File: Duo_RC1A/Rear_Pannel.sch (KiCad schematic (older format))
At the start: 61 parts, among them CN1 CONN_PANNEL, CN2 CONN_PANNEL, CN3 CONN_PANNEL, J10 MIDI_CONN, J11 JACK_3P_2.5MM, J6 USB_A, J7 MINI_USB_OTG, J8 RJ45_CHAIN, J9 MIDI_CONN, Q4 BS870, Q5 BS870, U5 RT9728BH, U6 RT9728BH, U7 6N137

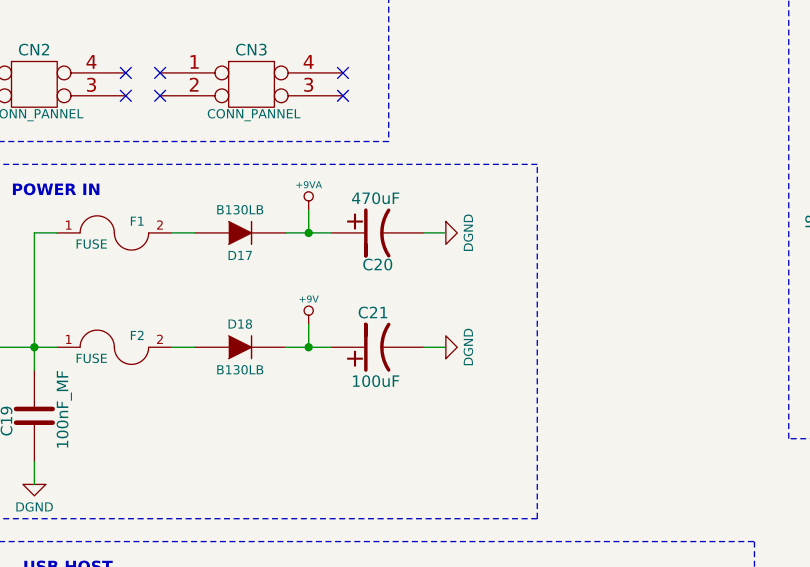
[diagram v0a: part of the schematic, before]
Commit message: PCB dimensions and group placement of all footprints on both BottomBoard and TopBoard layouts.
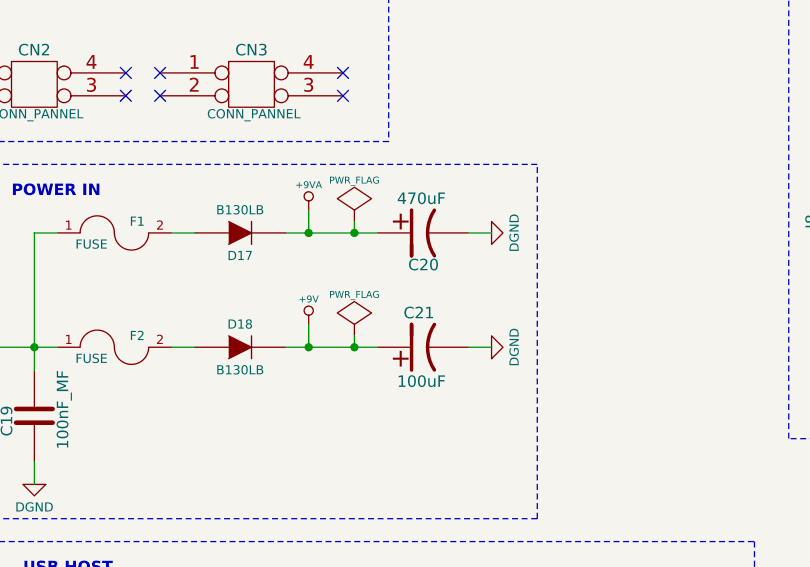
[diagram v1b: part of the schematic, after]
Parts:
- F1, F2: footprint Duo_Audio_HMI_RC1A:SM0603 -> Duo_Audio_HMI_RC1A:SM2920
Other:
- moved on the sheet: C20, C21

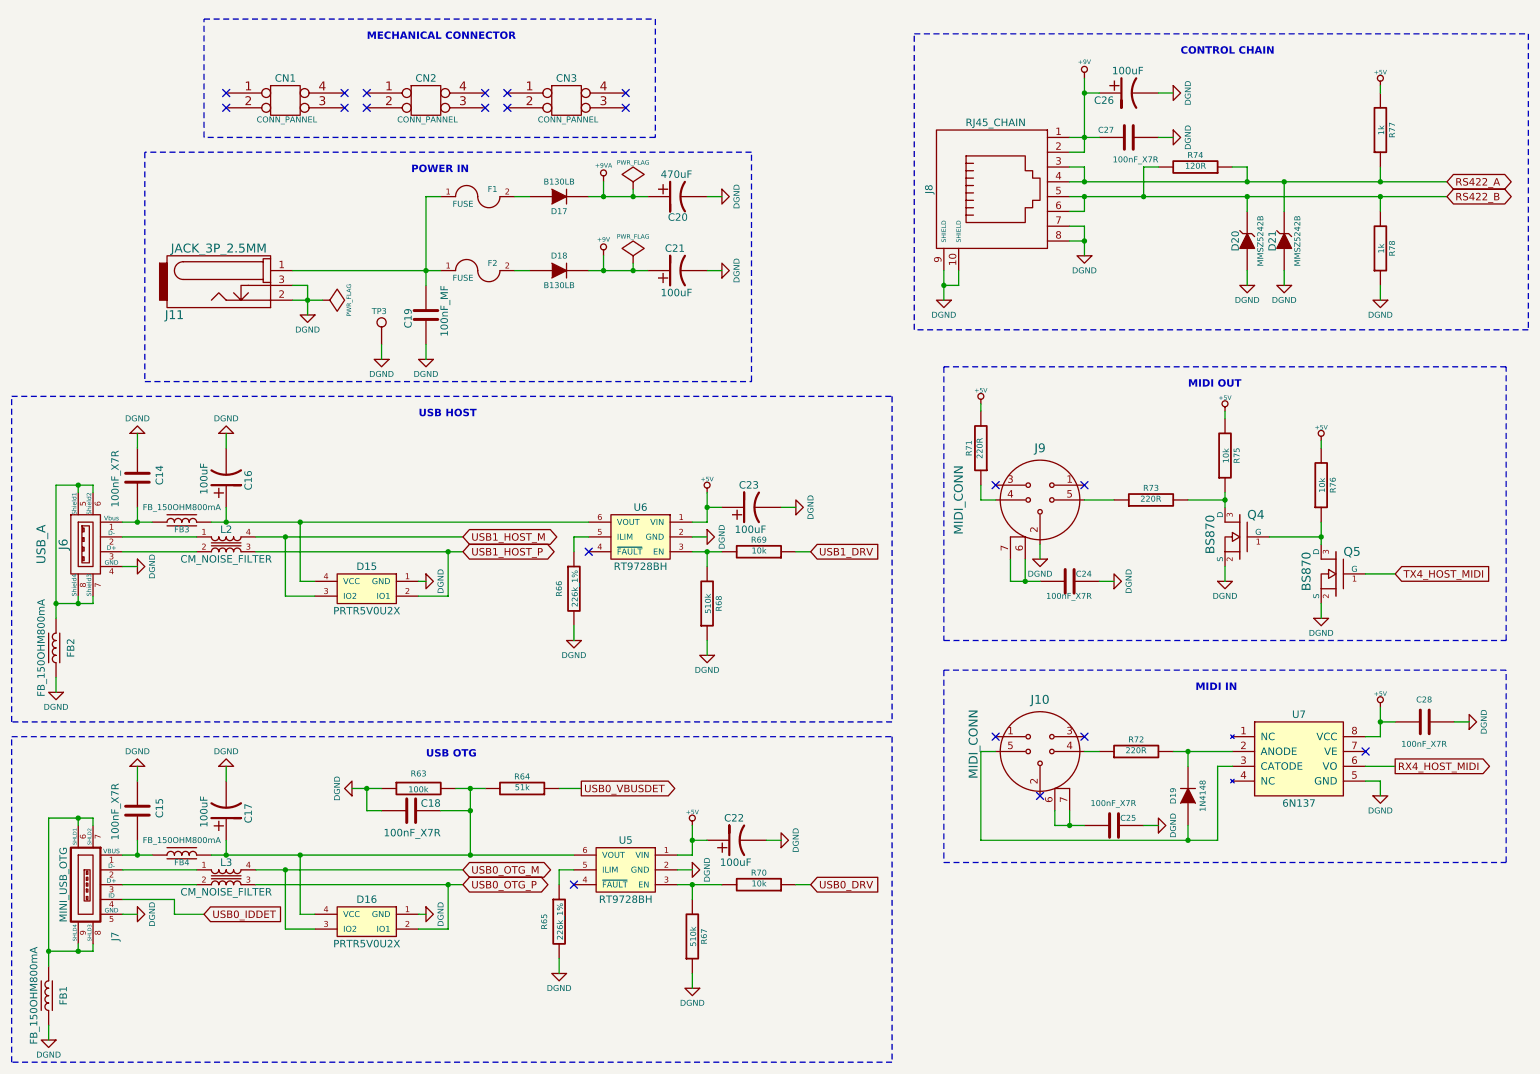
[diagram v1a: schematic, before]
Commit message: Working on the BottomBoard layout. Moved the ITEAD Coreboard to the board left side so there is more space for the linear regulators. Stopped on the USB OTG and USB Host layout.
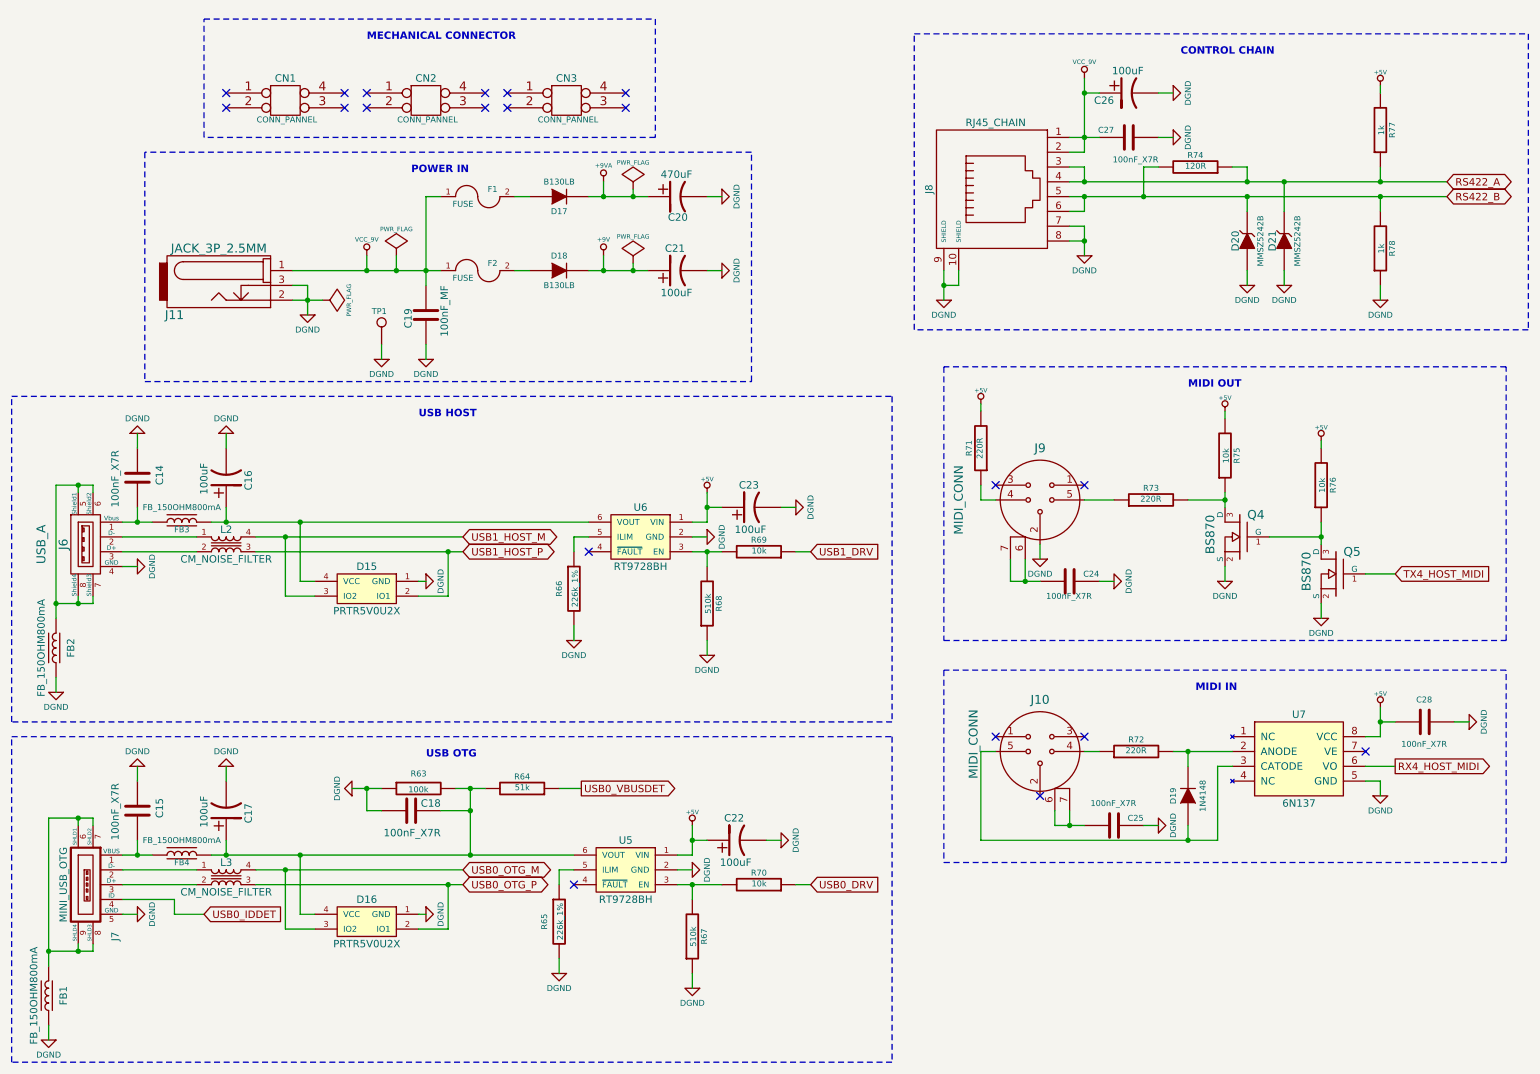
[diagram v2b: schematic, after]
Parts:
- renumbered TP3 to TP1
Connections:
- net +9V: no longer C26.1, C27.1, J8.1, J8.2
- net VCC_9V: now reaches C19.2, F1.1, F2.1, J11.1
- net VCC_9V: now also C26.1, C27.1, J8.1, J8.2

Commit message: Rear pannel layout finished. First layout of sound modules.
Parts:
- TP1: footprint Duo_Audio_HMI_RC1A:TESTPOINT_2.2MM -> Duo_Audio_HMI_RC1A:TESTPOINT_1MM

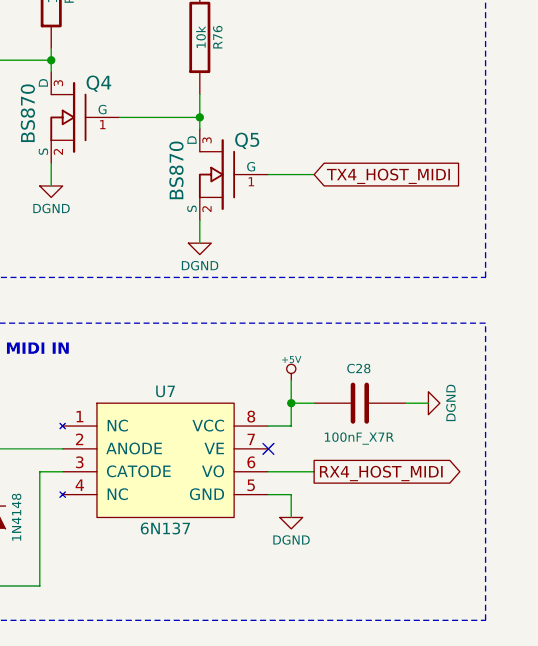
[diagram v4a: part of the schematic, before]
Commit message: Removed CODEC_MITEC signal. Defined the connector between the TopBoard and the BottomBoard. Saved layouts in *.brd old format.
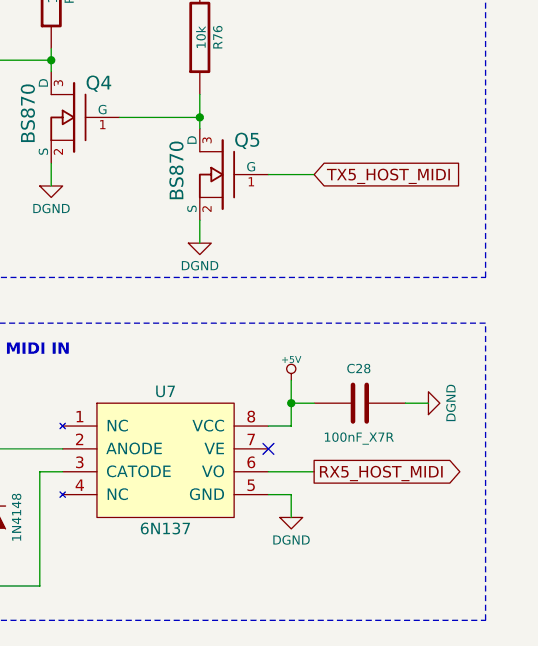
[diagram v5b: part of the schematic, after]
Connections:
- net RX4_HOST_MIDI renamed RX5_HOST_MIDI
- net TX4_HOST_MIDI renamed TX5_HOST_MIDI

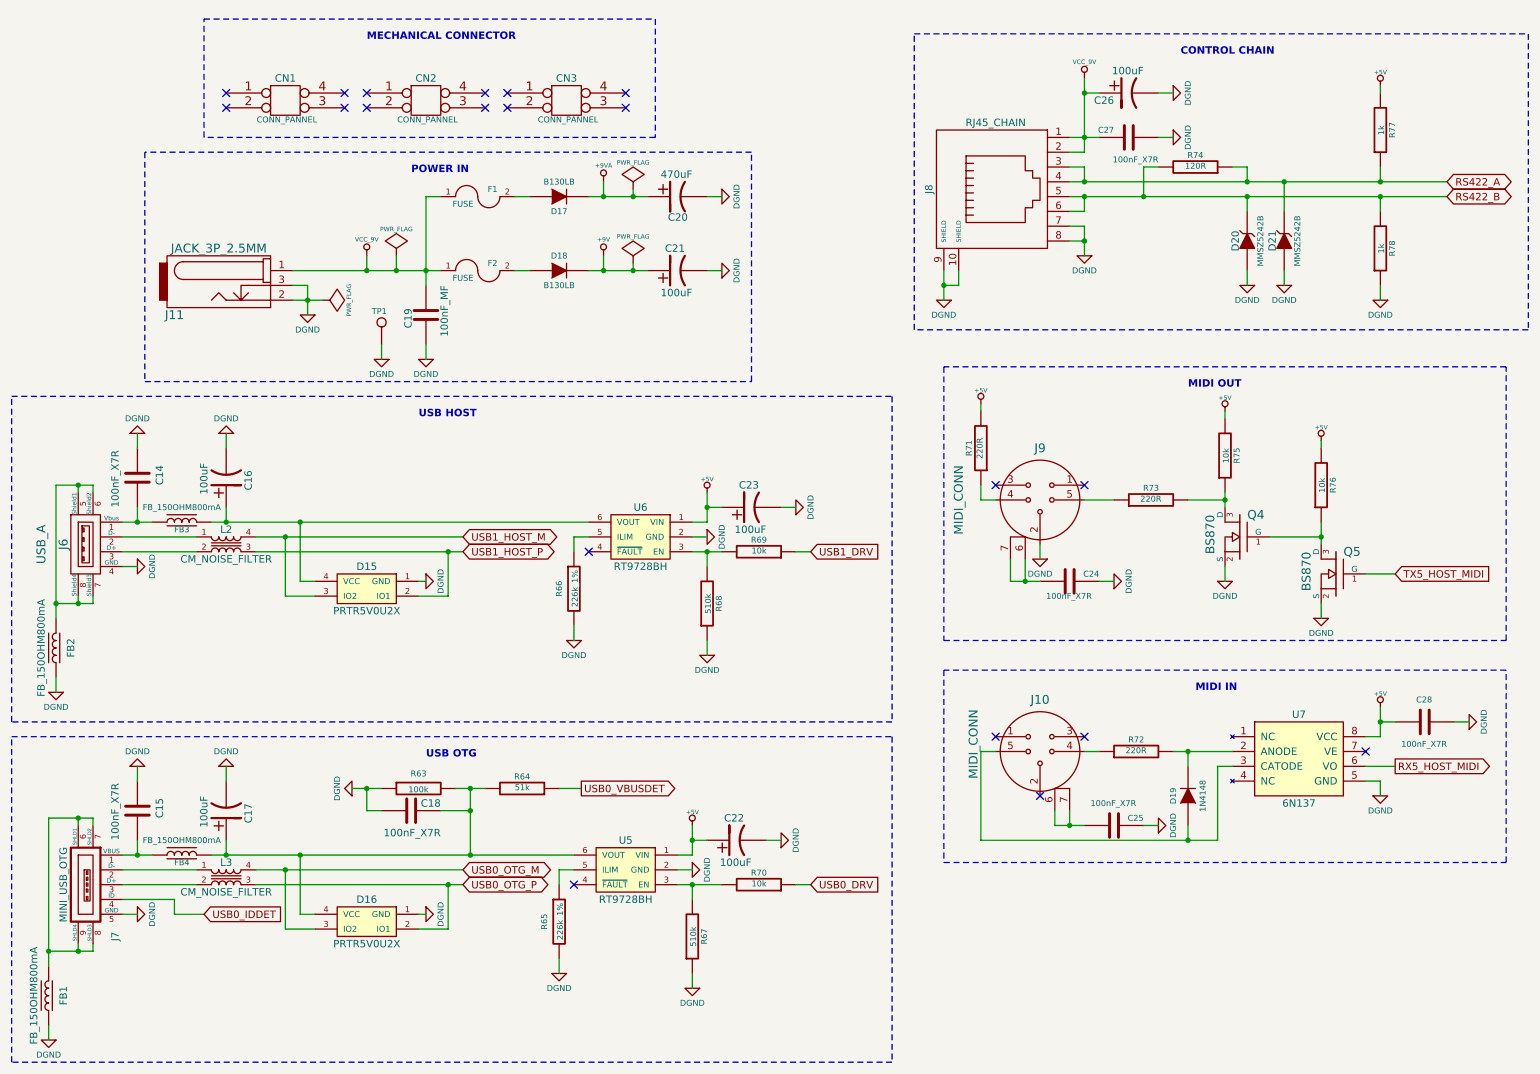
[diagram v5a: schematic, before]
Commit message: Changed the LCD for the 2.8pol. Rotated the bottom board connector. Moved the 3.3V linear regulator from the bottom board to the top board, and changed the power for the top board from 3.3V to 9V.
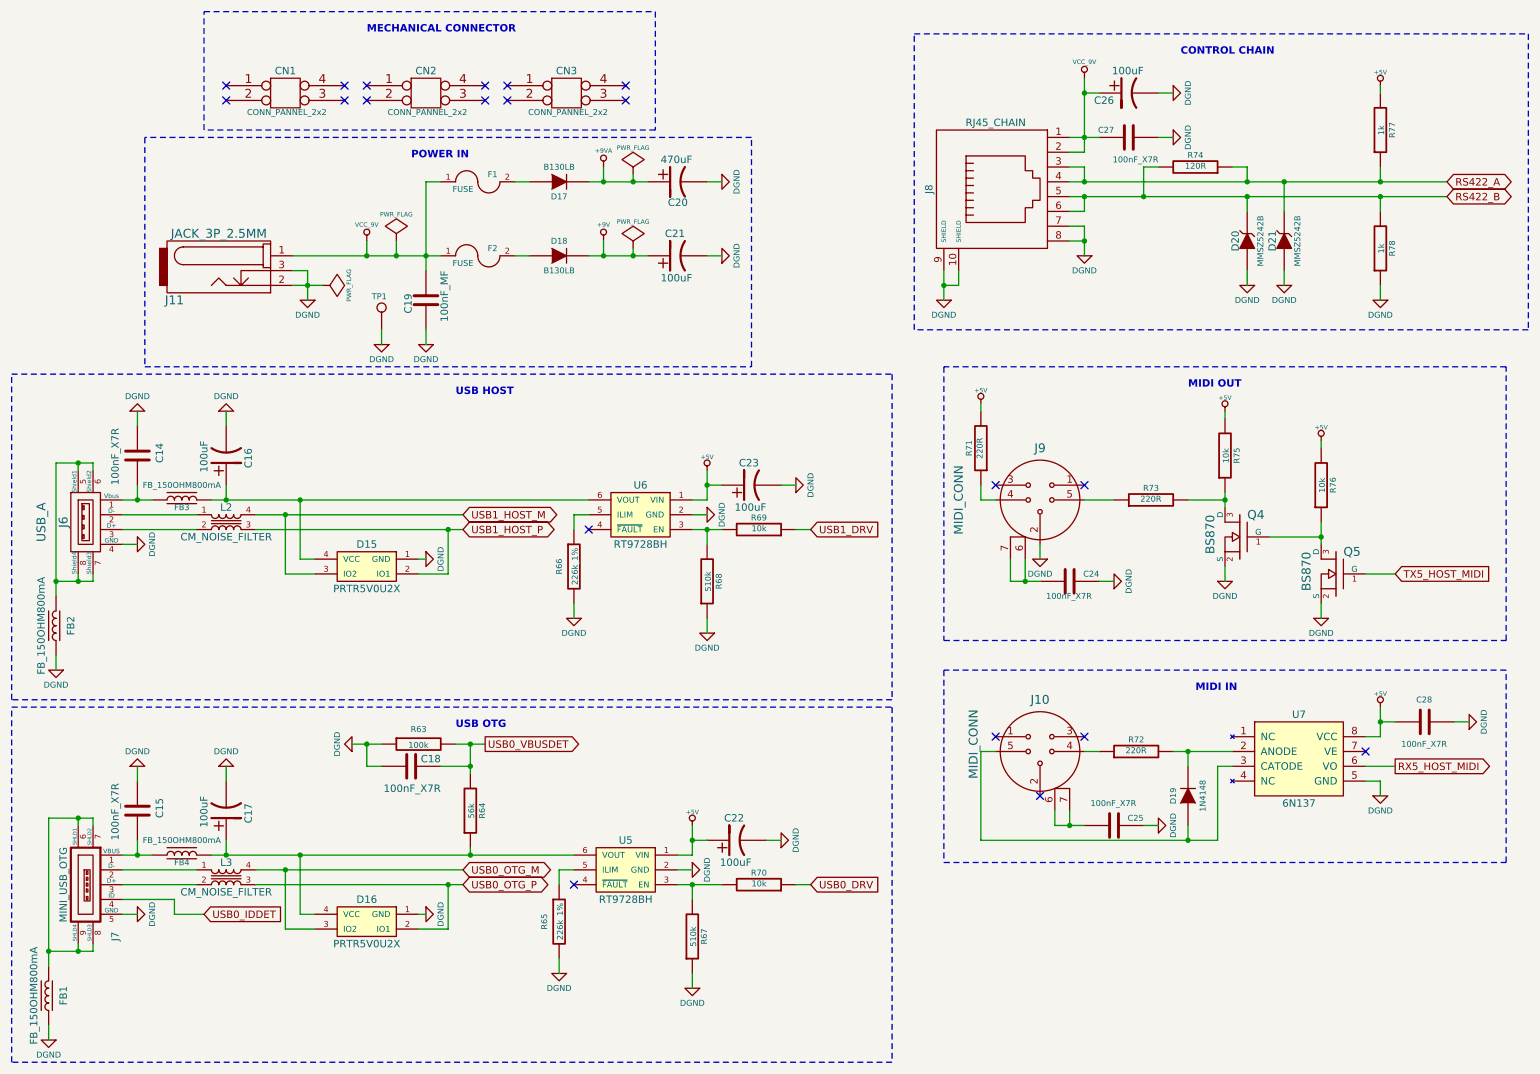
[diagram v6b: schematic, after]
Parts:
- CN1, CN2, CN3: value CONN_PANNEL -> CONN_PANNEL_2x2
- R64: value 51k -> 56k
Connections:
- net USB0_VBUSDET: now also C18.2, R63.2, R64.2; no longer R64.1
- net at C17.1, D16.4 (VCC), FB4.2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: now also R64.1; no longer C18.2, R63.2, R64.2
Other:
- moved on the sheet: C14, C16, C18, C19, C20, C21, C23, CN1, CN2, CN3, D15, D17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

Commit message: Wrking on the sound. Changed the board size.
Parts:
- added TP3: TEST_POINT_2MM, Duo_Audio_HMI_RC1A:TESTPOINT_2.2MM, symbol CONN_1
- TP1: footprint Duo_Audio_HMI_RC1A:TESTPOINT_1MM -> Duo_Audio_HMI_RC1A:TESTPOINT_2.2MM
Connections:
- new net AGND: TP3.1
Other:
- moved on the sheet: TP1
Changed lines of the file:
@@
 L CONN_1 TP1
 U 1 1 537BD963
-P 3250 2550
-F 0 "TP1" V 3325 2515 40  0000 L CNN
-F 1 "TEST_POINT_2MM" H 3250 2605 30  0001 C CNN
-F 2 "Duo_Audio_HMI_RC1A:TESTPOINT_1MM" H 3250 2550 60  0001 C CNN
-F 3 "" H 3250 2550 60  0000 C CNN
-	1    3250 2550
+P 2100 1550
+F 0 "TP1" V 2175 1515 40  0000 L CNN
+F 1 "TEST_POINT_2MM" H 2100 1605 30  0001 C CNN
+F 2 "Duo_Audio_HMI_RC1A:TESTPOINT_2.2MM" H 2100 1550 60  0001 C CNN
+F 3 "" H 2100 1550 60  0000 C CNN
+	1    2100 1550
 	0    -1   -1   0
 $EndComp
@@
 L DGND #PWR0250
 U 1 1 537BD964
-P 3250 2800
-F 0 "#PWR0250" H 3250 2800 40  0001 C CNN
-F 1 "DGND" H 3250 2700 40  0000 C CNN
-F 2 "~" H 3250 2800 60  0000 C CNN
-F 3 "~" H 3250 2800 60  0000 C CNN
-	1    3250 2800
+P 2100 1800
+F 0 "#PWR0250" H 2100 1800 40  0001 C CNN
+F 1 "DGND" H 2100 1700 40  0000 C CNN
+F 2 "~" H 2100 1800 60  0000 C CNN
+F 3 "~" H 2100 1800 60  0000 C CNN
+	1    2100 1800
 	-1   0    0    -1
 $EndComp
@@
 Connection ~ 4750 1700
 Wire Wire Line
-	3250 2700 3250 2800
+	2100 1700 2100 1800
 Wire Wire Line
 	3550 1700 3550 2300
@@
 Wire Wire Line
 	3850 6200 3850 6250
+$Comp
+L CONN_1 TP3
+U 1 1 53C99717
+P 2550 1550
+F 0 "TP3" V 2625 1515 40  0000 L CNN
+F 1 "TEST_POINT_2MM" H 2550 1605 30  0001 C CNN
+F 2 "Duo_Audio_HMI_RC1A:TESTPOINT_2.2MM" H 2550 1550 60  0001 C CNN
+F 3 "" H 2550 1550 60  0000 C CNN
+	1    2550 1550
+	0    -1   -1   0
+$EndComp
+Wire Wire Line
+	2550 1700 2550 1800
+$Comp
+L AGND #PWR0259
+U 1 1 53C9973A
+P 2550 1800
+F 0 "#PWR0259" H 2550 1800 40  0001 C CNN
+F 1 "AGND" H 2550 1730 50  0000 C CNN
+F 2 "" H 2550 1800 60  0000 C CNN
+F 3 "" H 2550 1800 60  0000 C CNN
+	1    2550 1800
+	1    0    0    -1
+$EndComp
 $EndSCHEMATC
